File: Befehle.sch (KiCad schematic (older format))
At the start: 52 parts, among them P1 CONN_02X10, P2 CONN_02X10, U1 74LS14, U2 74540, U3 7400, U4 74HCT02, U5 74LS541, U6 74LS373, U7 74LS139, U8 74LS540

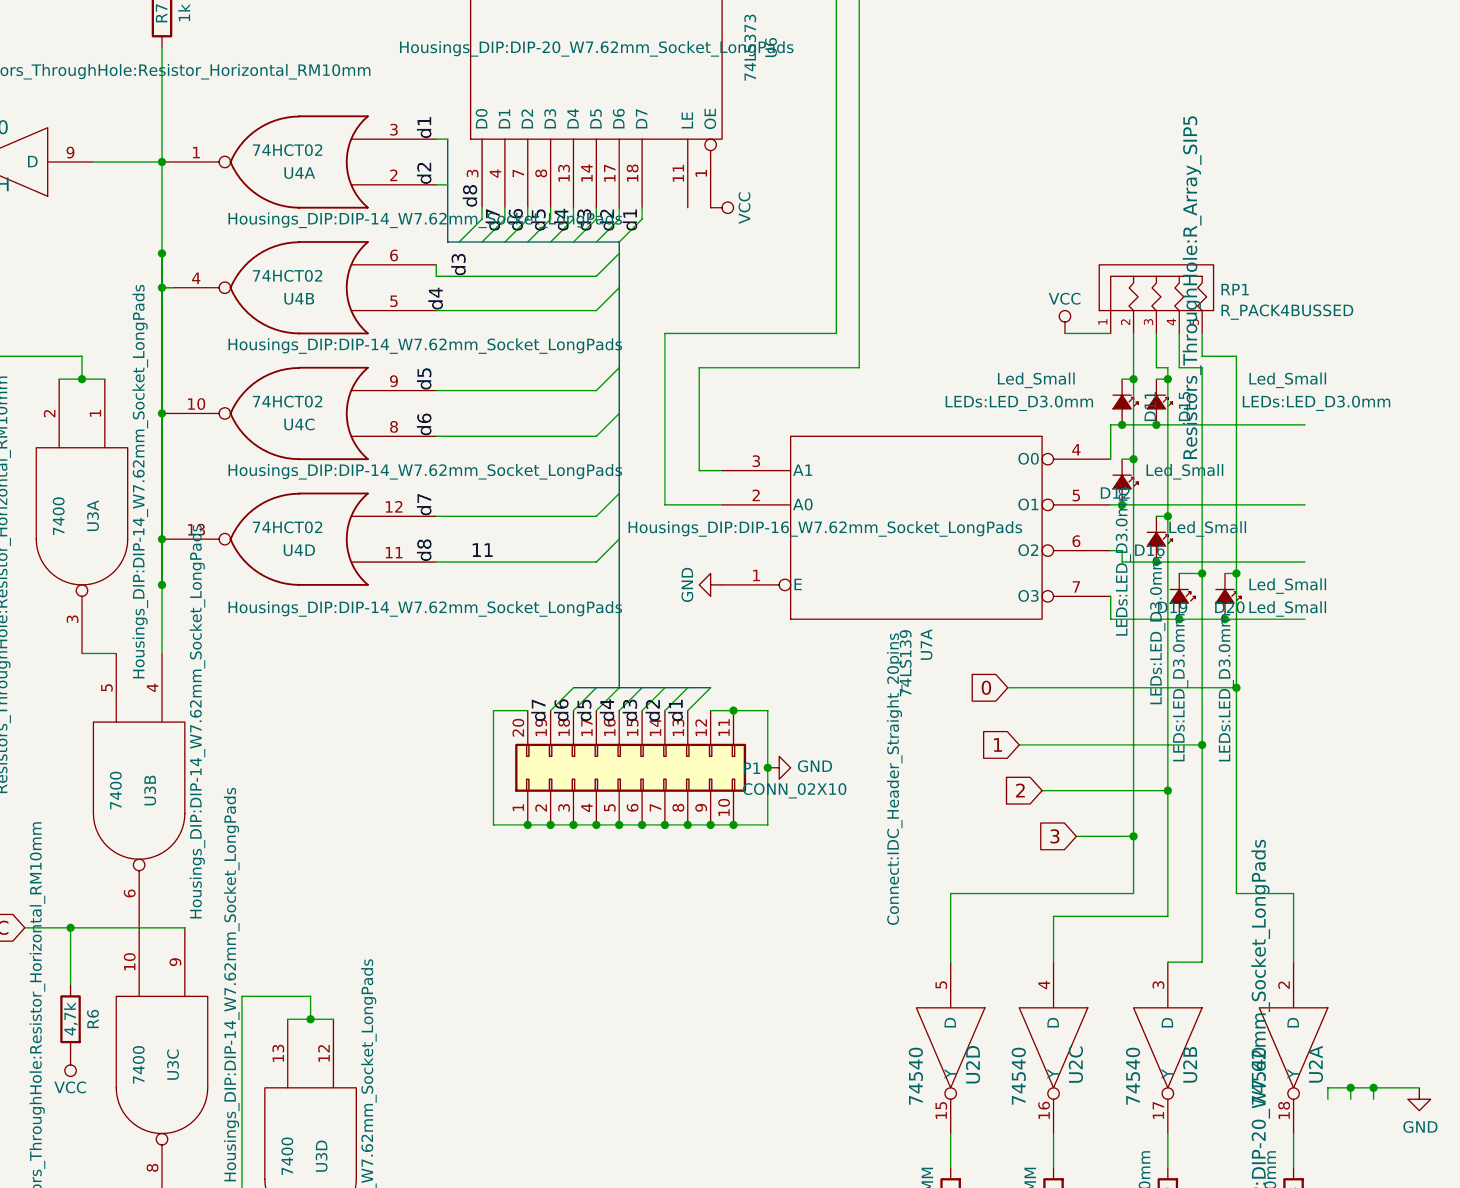
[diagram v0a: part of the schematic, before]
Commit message: diodes under res array Befehle are now smaler
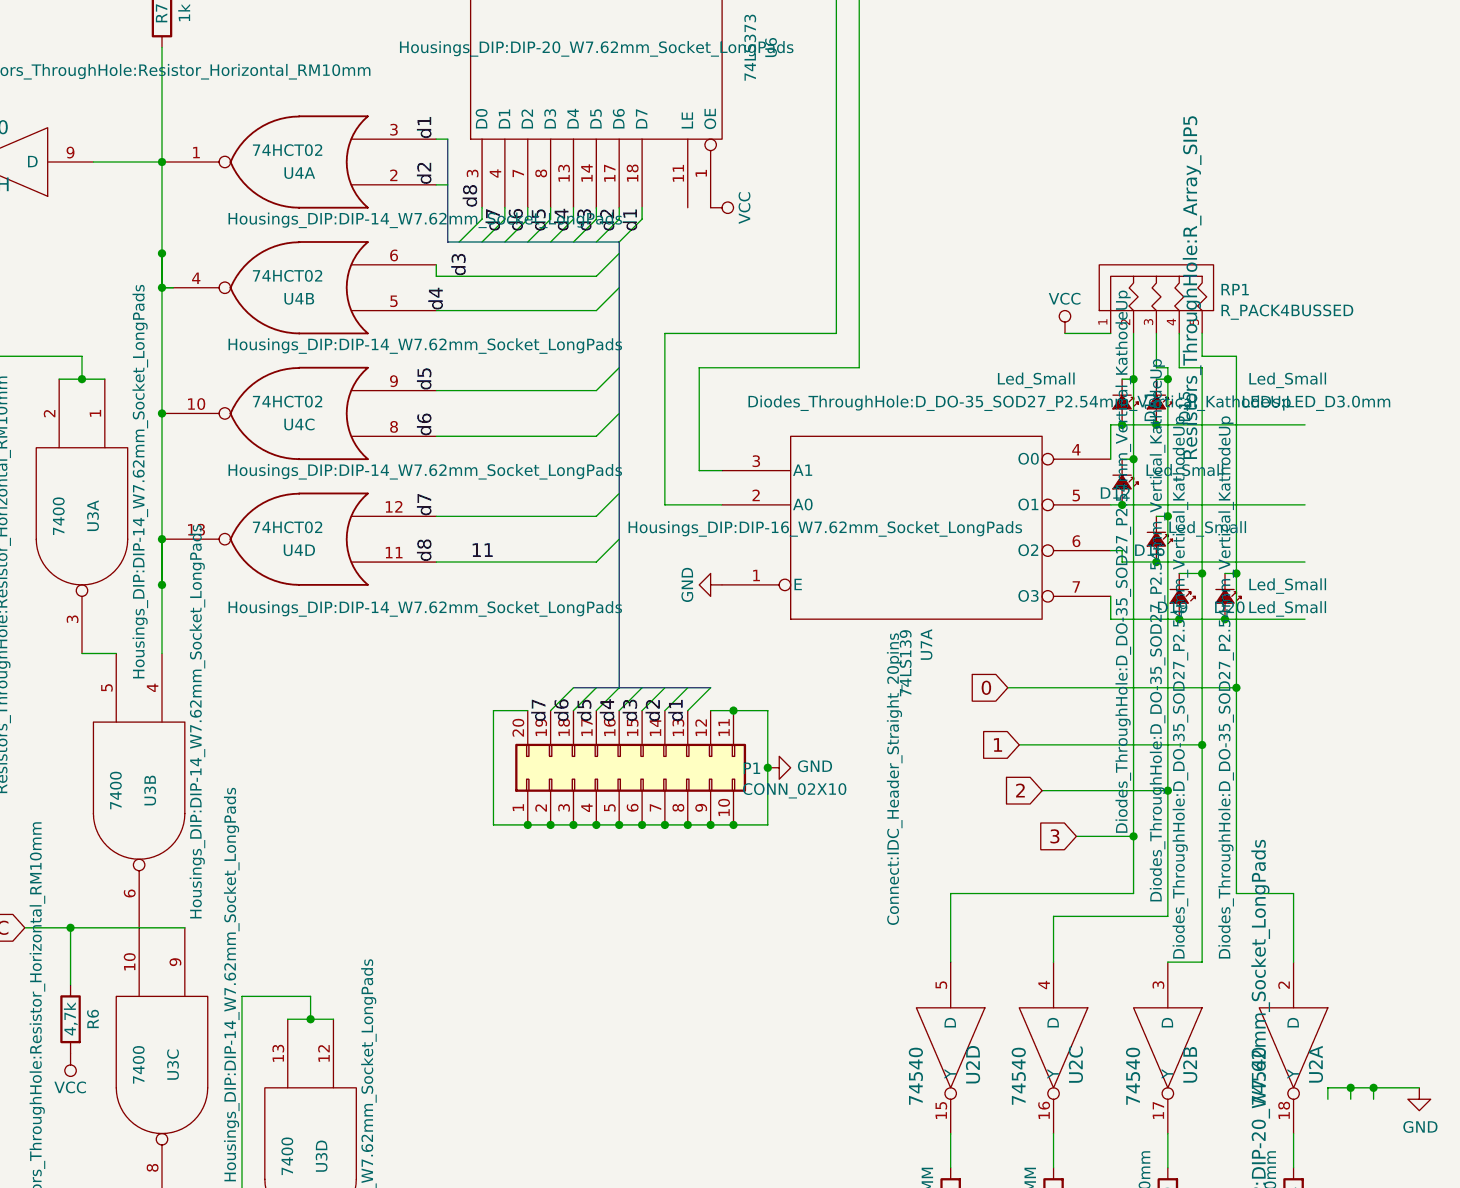
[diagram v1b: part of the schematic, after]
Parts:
- D11, D12, D16, D19, D20: footprint LEDs:LED_D3.0mm -> Diodes_ThroughHole:D_DO-35_SOD27_P2.54mm_Vertical_KathodeUp
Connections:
- wire segments 263 -> 259
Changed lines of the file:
@@
 F 0 "D11" H -4150 5675 50  0000 L CNN
 F 1 "Led_Small" V -4200 5000 50  0000 L CNN
-F 2 "LEDs:LED_D3.0mm" V -4100 5100 50  0000 C CNN
+F 2 "Diodes_ThroughHole:D_DO-35_SOD27_P2.54mm_Vertical_KathodeUp" V -4100 5100 50  0000 C CNN
 F 3 "" V -4100 5550 50  0000 C CNN
 	1    -4100 5550
@@
 F 0 "D12" V -4050 5800 50  0000 L CNN
 F 1 "Led_Small" V -4150 6000 50  0000 L CNN
-F 2 "LEDs:LED_D3.0mm" H -3750 5900 50  0000 C CNN
+F 2 "Diodes_ThroughHole:D_DO-35_SOD27_P2.54mm_Vertical_KathodeUp" H -3750 5900 50  0000 C CNN
 F 3 "" V -4100 5900 50  0000 C CNN
 	1    -4100 5900
@@
 F 0 "D16" V -3900 6050 50  0000 L CNN
 F 1 "Led_Small" V -4000 6200 50  0000 L CNN
-F 2 "LEDs:LED_D3.0mm" H -3550 6150 50  0000 C CNN
+F 2 "Diodes_ThroughHole:D_DO-35_SOD27_P2.54mm_Vertical_KathodeUp" H -3550 6150 50  0000 C CNN
 F 3 "" V -3950 6150 50  0000 C CNN
 	1    -3950 6150
@@
 F 0 "D20" V -3600 6350 50  0000 L CNN
 F 1 "Led_Small" V -3700 6500 50  0000 L CNN
-F 2 "LEDs:LED_D3.0mm" H -3250 6400 50  0000 C CNN
+F 2 "Diodes_ThroughHole:D_DO-35_SOD27_P2.54mm_Vertical_KathodeUp" H -3250 6400 50  0000 C CNN
 F 3 "" V -3650 6400 50  0000 C CNN
 	1    -3650 6400
@@
 F 0 "D19" V -3800 6300 50  0000 L CNN
 F 1 "Led_Small" V -3800 6700 50  0000 L CNN
-F 2 "LEDs:LED_D3.0mm" H -3450 6400 50  0000 C CNN
+F 2 "Diodes_ThroughHole:D_DO-35_SOD27_P2.54mm_Vertical_KathodeUp" H -3450 6400 50  0000 C CNN
 F 3 "" V -3850 6400 50  0000 C CNN
 	1    -3850 6400
@@
 Wire Wire Line
 	-8300 5050 -8300 5600
-Wire Wire Line
-	-8300 6350 -8300 6150
-Wire Wire Line
-	-8300 5050 -8300 4900
-Wire Wire Line
-	-8300 4500 -8300 4900
-Wire Bus Line
-	-6500 6800 -6300 6800
-Wire Bus Line
-	-6300 6800 -5900 6800
-Wire Bus Line
-	-4650 1950 -3950 1950
-Wire Bus Line
-	-6900 2650 -3950 2650
-Wire Bus Line
-	-6300 4850 -6300 6800
-Wire Bus Line
-	-7050 4850 -6300 4850
 Connection ~ -8300 6350
-Wire Wire Line
-	-8300 6350 -8300 6650
 Connection ~ -8300 4900
 Wire Wire Line
@@
 Wire Wire Line
 	-8300 5600 -8300 6150
-Wire Wire Line
-	-8300 5600 -8300 5050
 Connection ~ -8300 6150
 Wire Wire Line
-	-8300 6150 -8300 5600
-Wire Wire Line
 	-8300 6150 -8300 6350
+Wire Wire Line
+	-8300 6150 -8300 6650
+Wire Wire Line
+	-8300 4500 -8300 5050
+Wire Bus Line
+	-6500 6800 -6300 6800
+Wire Bus Line
+	-6300 6800 -5900 6800
+Wire Bus Line
+	-4650 1950 -3950 1950
+Wire Bus Line
+	-6900 2650 -3950 2650
+Wire Bus Line
+	-6300 4850 -6300 6800
+Wire Bus Line
+	-7050 4850 -6300 4850
 $EndSCHEMATC

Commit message: resistoren footprint ausgetsauscht (nicht fertig)
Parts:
- R10, R11, R12, R13, R14, R15, R16, R18, R20, R21, R24, R9: footprint Resistors_ThroughHole:R_Axial_DIN0204_L3.6mm_D1.6mm_P5.08mm_Horizontal -> Resistors_ThroughHole:R_Axial_DIN0207_L6.3mm_D2.5mm_P10.16mm_Horizontal
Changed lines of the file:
@@
 F 0 "R10" V -4550 200 50  0000 C CNN
 F 1 "330" V -4550 350 50  0000 C CNN
-F 2 "Resistors_ThroughHole:R_Axial_DIN0204_L3.6mm_D1.6mm_P5.08mm_Horizontal" V -4550 -1750 50  0000 C CNN
+F 2 "Resistors_ThroughHole:R_Axial_DIN0207_L6.3mm_D2.5mm_P10.16mm_Horizontal" V -4550 -1750 50  0000 C CNN
 F 3 "" H -4550 200 50  0000 C CNN
 	1    -4550 200
@@
 F 0 "R11" V -4450 200 50  0000 C CNN
 F 1 "330" V -4450 350 50  0000 C CNN
-F 2 "Resistors_ThroughHole:R_Axial_DIN0204_L3.6mm_D1.6mm_P5.08mm_Horizontal" V -4450 -1750 50  0000 C CNN
+F 2 "Resistors_ThroughHole:R_Axial_DIN0207_L6.3mm_D2.5mm_P10.16mm_Horizontal" V -4450 -1750 50  0000 C CNN
 F 3 "" H -4450 200 50  0000 C CNN
 	1    -4450 200
@@
 F 0 "R13" V -4350 200 50  0000 C CNN
 F 1 "330" V -4350 350 50  0000 C CNN
-F 2 "Resistors_ThroughHole:R_Axial_DIN0204_L3.6mm_D1.6mm_P5.08mm_Horizontal" V -4350 -1750 50  0000 C CNN
+F 2 "Resistors_ThroughHole:R_Axial_DIN0207_L6.3mm_D2.5mm_P10.16mm_Horizontal" V -4350 -1750 50  0000 C CNN
 F 3 "" H -4350 200 50  0000 C CNN
 	1    -4350 200
@@
 F 0 "R14" V -4250 200 50  0000 C CNN
 F 1 "330" V -4250 350 50  0000 C CNN
-F 2 "Resistors_ThroughHole:R_Axial_DIN0204_L3.6mm_D1.6mm_P5.08mm_Horizontal" V -4250 -1750 50  0000 C CNN
+F 2 "Resistors_ThroughHole:R_Axial_DIN0207_L6.3mm_D2.5mm_P10.16mm_Horizontal" V -4250 -1750 50  0000 C CNN
 F 3 "" H -4250 200 50  0000 C CNN
 	1    -4250 200
@@
 F 0 "R15" V -4150 200 50  0000 C CNN
 F 1 "330" V -4150 350 50  0000 C CNN
-F 2 "Resistors_ThroughHole:R_Axial_DIN0204_L3.6mm_D1.6mm_P5.08mm_Horizontal" V -4150 -1750 50  0000 C CNN
+F 2 "Resistors_ThroughHole:R_Axial_DIN0207_L6.3mm_D2.5mm_P10.16mm_Horizontal" V -4150 -1750 50  0000 C CNN
 F 3 "" H -4150 200 50  0000 C CNN
 	1    -4150 200
@@
 F 0 "R16" V -4050 200 50  0000 C CNN
 F 1 "330" V -4050 350 50  0000 C CNN
-F 2 "Resistors_ThroughHole:R_Axial_DIN0204_L3.6mm_D1.6mm_P5.08mm_Horizontal" V -4050 -1750 50  0000 C CNN
+F 2 "Resistors_ThroughHole:R_Axial_DIN0207_L6.3mm_D2.5mm_P10.16mm_Horizontal" V -4050 -1750 50  0000 C CNN
 F 3 "" H -4050 200 50  0000 C CNN
 	1    -4050 200
@@
 F 0 "R18" V -3950 200 50  0000 C CNN
 F 1 "330" V -3950 350 50  0000 C CNN
-F 2 "Resistors_ThroughHole:R_Axial_DIN0204_L3.6mm_D1.6mm_P5.08mm_Horizontal" V -3950 -1750 50  0000 C CNN
+F 2 "Resistors_ThroughHole:R_Axial_DIN0207_L6.3mm_D2.5mm_P10.16mm_Horizontal" V -3950 -1750 50  0000 C CNN
 F 3 "" H -3950 200 50  0000 C CNN
 	1    -3950 200
@@
 F 0 "R21" V -3850 200 50  0000 C CNN
 F 1 "330" V -3850 350 50  0000 C CNN
-F 2 "Resistors_ThroughHole:R_Axial_DIN0204_L3.6mm_D1.6mm_P5.08mm_Horizontal" V -3850 -1750 50  0000 C CNN
+F 2 "Resistors_ThroughHole:R_Axial_DIN0207_L6.3mm_D2.5mm_P10.16mm_Horizontal" V -3850 -1750 50  0000 C CNN
 F 3 "" H -3850 200 50  0000 C CNN
 	1    -3850 200
@@
 F 0 "R24" V -3350 9050 50  0000 C CNN
 F 1 "330" V -3450 9050 50  0000 C CNN
-F 2 "Resistors_ThroughHole:R_Axial_DIN0204_L3.6mm_D1.6mm_P5.08mm_Horizontal" V -3350 11150 50  0000 C CNN
+F 2 "Resistors_ThroughHole:R_Axial_DIN0207_L6.3mm_D2.5mm_P10.16mm_Horizontal" V -3350 11150 50  0000 C CNN
 F 3 "" H -3350 9050 50  0000 C CNN
 	1    -3350 9050
@@
 F 0 "R20" V -3900 9050 50  0000 C CNN
 F 1 "330" V -4000 9050 50  0000 C CNN
-F 2 "Resistors_ThroughHole:R_Axial_DIN0204_L3.6mm_D1.6mm_P5.08mm_Horizontal" V -3900 11150 50  0000 C CNN
+F 2 "Resistors_ThroughHole:R_Axial_DIN0207_L6.3mm_D2.5mm_P10.16mm_Horizontal" V -3900 11150 50  0000 C CNN
 F 3 "" H -3900 9050 50  0000 C CNN
 	1    -3900 9050
@@
 F 0 "R12" V -4400 9050 50  0000 C CNN
 F 1 "330" V -4500 9050 50  0000 C CNN
-F 2 "Resistors_ThroughHole:R_Axial_DIN0204_L3.6mm_D1.6mm_P5.08mm_Horizontal" V -4400 11150 50  0000 C CNN
+F 2 "Resistors_ThroughHole:R_Axial_DIN0207_L6.3mm_D2.5mm_P10.16mm_Horizontal" V -4400 11150 50  0000 C CNN
 F 3 "" H -4400 9050 50  0000 C CNN
 	1    -4400 9050
@@
 F 0 "R9" V -4850 9050 50  0000 C CNN
 F 1 "330" V -4950 9050 50  0000 C CNN
-F 2 "Resistors_ThroughHole:R_Axial_DIN0204_L3.6mm_D1.6mm_P5.08mm_Horizontal" V -4850 11150 50  0000 C CNN
+F 2 "Resistors_ThroughHole:R_Axial_DIN0207_L6.3mm_D2.5mm_P10.16mm_Horizontal" V -4850 11150 50  0000 C CNN
 F 3 "" H -4850 9050 50  0000 C CNN
 	1    -4850 9050

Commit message: shizzl dizzl
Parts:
- R1, R2, R3, R4, R5, R6, R7, R8: footprint Resistors_ThroughHole:Resistor_Horizontal_RM10mm -> Resistors_ThroughHole:R_Axial_DIN0207_L6.3mm_D2.5mm_P10.16mm_Horizontal
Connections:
- wire segments 259 -> 258
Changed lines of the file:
@@
 F 0 "R7" V -8300 3850 50  0000 C CNN
 F 1 "1k" V -8400 3850 50  0000 C CNN
-F 2 "Resistors_ThroughHole:Resistor_Horizontal_RM10mm" H -8300 4100 50  0000 C CNN
+F 2 "Resistors_ThroughHole:R_Axial_DIN0207_L6.3mm_D2.5mm_P10.16mm_Horizontal" H -8300 4100 50  0000 C CNN
 F 3 "" H -8300 3850 50  0000 C CNN
 	1    -8300 3850
@@
 F 0 "R5" V -8800 2000 50  0000 C CNN
 F 1 "330" V -8900 2000 50  0000 C CNN
-F 2 "Resistors_ThroughHole:Resistor_Horizontal_RM10mm" V -9100 2050 50  0000 C CNN
+F 2 "Resistors_ThroughHole:R_Axial_DIN0207_L6.3mm_D2.5mm_P10.16mm_Horizontal" V -9100 2050 50  0000 C CNN
 F 3 "" H -8800 2000 50  0000 C CNN
 	1    -8800 2000
@@
 F 0 "R1" V -9700 1100 50  0000 C CNN
 F 1 "4,7k" V -9800 1100 50  0000 C CNN
-F 2 "Resistors_ThroughHole:Resistor_Horizontal_RM10mm" V -9500 2050 50  0000 C CNN
+F 2 "Resistors_ThroughHole:R_Axial_DIN0207_L6.3mm_D2.5mm_P10.16mm_Horizontal" V -9500 2050 50  0000 C CNN
 F 3 "" H -9700 1100 50  0000 C CNN
 	1    -9700 1100
@@
 F 0 "R6" V -8800 8250 50  0000 C CNN
 F 1 "4,7k" V -8700 8250 50  0000 C CNN
-F 2 "Resistors_ThroughHole:Resistor_Horizontal_RM10mm" V -8550 8200 50  0000 C CNN
+F 2 "Resistors_ThroughHole:R_Axial_DIN0207_L6.3mm_D2.5mm_P10.16mm_Horizontal" V -8550 8200 50  0000 C CNN
 F 3 "" H -8700 8250 50  0000 C CNN
 	1    -8700 8250
@@
 F 0 "R3" V -9070 5750 50  0000 C CNN
 F 1 "4,7k" V -9150 5750 50  0000 C CNN
-F 2 "Resistors_ThroughHole:Resistor_Horizontal_RM10mm" V -9300 5150 50  0000 C CNN
+F 2 "Resistors_ThroughHole:R_Axial_DIN0207_L6.3mm_D2.5mm_P10.16mm_Horizontal" V -9300 5150 50  0000 C CNN
 F 3 "" H -9150 5750 50  0000 C CNN
 	1    -9150 5750
@@
 F 0 "R2" V -9350 4650 50  0000 C CNN
 F 1 "330" V -9450 4650 50  0000 C CNN
-F 2 "Resistors_ThroughHole:Resistor_Horizontal_RM10mm" V -9150 3850 50  0000 C CNN
+F 2 "Resistors_ThroughHole:R_Axial_DIN0207_L6.3mm_D2.5mm_P10.16mm_Horizontal" V -9150 3850 50  0000 C CNN
 F 3 "" H -9350 4650 50  0000 C CNN
 	1    -9350 4650
@@
 F 0 "R4" V -8950 3450 50  0000 C CNN
 F 1 "4,7k" V -8850 3450 50  0000 C CNN
-F 2 "Resistors_ThroughHole:Resistor_Horizontal_RM10mm" H -9200 3650 50  0000 C CNN
+F 2 "Resistors_ThroughHole:R_Axial_DIN0207_L6.3mm_D2.5mm_P10.16mm_Horizontal" H -9200 3650 50  0000 C CNN
 F 3 "" H -8850 3450 50  0000 C CNN
 	1    -8850 3450
@@
 F 0 "R8" V -7400 2350 50  0000 C CNN
 F 1 "330" V -7500 2350 50  0000 C CNN
-F 2 "Resistors_ThroughHole:Resistor_Horizontal_RM10mm" H -7050 2100 50  0000 C CNN
+F 2 "Resistors_ThroughHole:R_Axial_DIN0207_L6.3mm_D2.5mm_P10.16mm_Horizontal" H -7050 2100 50  0000 C CNN
 F 3 "" H -7400 2350 50  0000 C CNN
 	1    -7400 2350
@@
 Wire Wire Line
 	-8300 5050 -8300 5600
-Connection ~ -8300 6350
-Connection ~ -8300 4900
-Wire Wire Line
-	-8300 4900 -8300 5050
 Connection ~ -8300 5600
 Wire Wire Line
@@
 Connection ~ -8300 6150
 Wire Wire Line
-	-8300 6150 -8300 6350
+	-8300 4900 -8300 5050
+Wire Wire Line
+	-8300 4500 -8300 5050
 Wire Wire Line
 	-8300 6150 -8300 6650
-Wire Wire Line
-	-8300 4500 -8300 5050
 Wire Bus Line
 	-6500 6800 -6300 6800

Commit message: shizzl
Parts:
- D1, D4, D7: footprint LEDs:LED-3MM -> LEDs:LED_D3.0mm
- D15: footprint LEDs:LED_D3.0mm -> Diodes_ThroughHole:D_DO-35_SOD27_P2.54mm_Vertical_KathodeUp
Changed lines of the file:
@@
 F 0 "D7" H -4400 9443 50  0000 C CNN
 F 1 "LED" H -4400 9186 50  0001 C CNN
-F 2 "LEDs:LED-3MM" H -4550 9200 50  0000 C CNN
+F 2 "LEDs:LED_D3.0mm" H -4550 9200 50  0000 C CNN
 F 3 "" V -4400 9300 50  0000 C CNN
 	1    -4400 9300
@@
 F 0 "D4" H -4850 9450 50  0000 C CNN
 F 1 "LED" H -4850 9186 50  0001 C CNN
-F 2 "LEDs:LED-3MM" H -5000 9200 50  0000 C CNN
+F 2 "LEDs:LED_D3.0mm" H -5000 9200 50  0000 C CNN
 F 3 "" V -4850 9300 50  0000 C CNN
 	1    -4850 9300
@@
 F 0 "D15" H -4000 5675 50  0000 L CNN
 F 1 "Led_Small" V -4050 5950 50  0000 L CNN
-F 2 "LEDs:LED_D3.0mm" V -3950 6250 50  0000 C CNN
+F 2 "Diodes_ThroughHole:D_DO-35_SOD27_P2.54mm_Vertical_KathodeUp" V -3950 6250 50  0000 C CNN
 F 3 "" V -3950 5550 50  0000 C CNN
 	1    -3950 5550
@@
 F 0 "D1" H -9350 5000 50  0000 C CNN
 F 1 "LED" H -9350 4786 50  0001 C CNN
-F 2 "LEDs:LED-3MM" V -9200 4900 50  0000 C CNN
+F 2 "LEDs:LED_D3.0mm" V -9200 4900 50  0000 C CNN
 F 3 "" V -9350 4900 50  0000 C CNN
 	1    -9350 4900

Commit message: diode und erste pins
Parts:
- added D22: D, Diodes_ThroughHole:D_DO-41_SOD81_P10.16mm_Horizontal, symbol device:D
- added J1: 691213710003, 691213710003, symbol PCB~Terminal~Blocks:691213710003
- added P3, P4: CONN_01X01, Pin_Headers:Pin_Header_Straight_1x01_Pitch1.27mm, symbol conn:CONN_01X01
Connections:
- wire segments 258 -> 278

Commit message: Kabel gelegt
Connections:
- wire segments 278 -> 258
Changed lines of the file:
@@
 EESchema Schematic File Version 4
-LIBS:Befehle-cache
 EELAYER 26 0
 EELAYER END
@@
 L power:VCC #PWR016
 U 1 1 57FC839A
-P -3200 9450
-F 0 "#PWR016" H -3200 9300 50  0001 C CNN
-F 1 "VCC" H -3200 9600 50  0000 C CNN
-F 2 "" H -3200 9450 50  0000 C CNN
-F 3 "" H -3200 9450 50  0000 C CNN
-	1    -3200 9450
-	0    1    1    0
+P -2900 8500
+F 0 "#PWR016" H -2900 8350 50  0001 C CNN
+F 1 "VCC" H -2900 8650 50  0000 C CNN
+F 2 "" H -2900 8500 50  0000 C CNN
+F 3 "" H -2900 8500 50  0000 C CNN
+	1    -2900 8500
+	1    0    0    -1
 $EndComp
 Text GLabel -4600 6800 0    60   Input ~ 0
@@
 	-3200 8600 -3200 8550
 Wire Wire Line
-	-3200 8550 -3100 8550
-Wire Wire Line
 	-3100 8600 -3100 8550
-Connection ~ -3100 8550
-Wire Wire Line
-	-3100 8550 -3000 8550
 Wire Wire Line
 	-3000 8600 -3000 8550
@@
 	-6850 6900 -6850 7400
 Wire Wire Line
-	-6850 7400 -6700 7400
-Wire Wire Line
 	-5650 7400 -5650 7150
-Wire Wire Line
-	-5650 6900 -5800 6900
-Connection ~ -6700 7400
-Wire Wire Line
-	-6700 7400 -6600 7400
-Connection ~ -6600 7400
-Wire Wire Line
-	-6600 7400 -6500 7400
-Connection ~ -6500 7400
-Wire Wire Line
-	-6500 7400 -6400 7400
-Connection ~ -6400 7400
-Wire Wire Line
-	-6400 7400 -6300 7400
-Connection ~ -6300 7400
-Wire Wire Line
-	-6300 7400 -6200 7400
-Connection ~ -6200 7400
-Wire Wire Line
-	-6200 7400 -6100 7400
-Connection ~ -6100 7400
-Wire Wire Line
-	-6100 7400 -6000 7400
-Connection ~ -6000 7400
-Wire Wire Line
-	-6000 7400 -5900 7400
-Connection ~ -5900 7400
-Wire Wire Line
-	-5900 7400 -5800 7400
-Connection ~ -5800 7400
-Wire Wire Line
-	-5800 7400 -5650 7400
-Connection ~ -5800 6900
-Wire Wire Line
-	-5800 6900 -5900 6900
 Wire Wire Line
 	-6850 6900 -6700 6900
@@
 	-6450 -550 -6550 -550
 Wire Wire Line
-	-6550 -1050 -6450 -1050
-Wire Wire Line
 	-5450 -1050 -5450 -800
 Wire Wire Line
@@
 Wire Wire Line
 	-6550 -1050 -6550 -550
-Connection ~ -6450 -1050
-Wire Wire Line
-	-6450 -1050 -6350 -1050
-Connection ~ -6350 -1050
-Wire Wire Line
-	-6350 -1050 -6250 -1050
-Connection ~ -6250 -1050
-Wire Wire Line
-	-6250 -1050 -6150 -1050
-Connection ~ -6150 -1050
-Wire Wire Line
-	-6150 -1050 -6050 -1050
-Connection ~ -6050 -1050
-Wire Wire Line
-	-6050 -1050 -5950 -1050
-Connection ~ -5950 -1050
-Wire Wire Line
-	-5950 -1050 -5850 -1050
-Connection ~ -5850 -1050
-Wire Wire Line
-	-5850 -1050 -5750 -1050
-Connection ~ -5750 -1050
-Wire Wire Line
-	-5750 -1050 -5650 -1050
-Connection ~ -5650 -1050
-Wire Wire Line
-	-5650 -1050 -5550 -1050
-Connection ~ -5550 -1050
-Wire Wire Line
-	-5550 -1050 -5450 -1050
 $Comp
 L power:GND #PWR019
@@
 Wire Wire Line
 	1100 4200 1100 4550
+Wire Wire Line
+	300  4200 300  4800
+Wire Wire Line
+	-5900 6900 -5650 6900
+Wire Wire Line
+	-6850 7400 -5650 7400
+Wire Wire Line
+	-6550 -1050 -5450 -1050
+Connection ~ -3100 8550
+Wire Wire Line
+	-3200 8550 -3100 8550
+Wire Wire Line
+	-3100 8550 -3000 8550
 Wire Bus Line
 	-6500 6800 -6300 6800
 Wire Wire Line
-	300  4200 300  4800
+	-2900 8500 -2900 8750
 Wire Bus Line
 	-6300 6800 -5900 6800
